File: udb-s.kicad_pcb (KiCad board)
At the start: 2 copper layers, 13 x 15.1 mm, 9 parts, among them J1 TYPE-C-31-M-12, J2 Conn_01x04, J3 Conn_01x04, U1 TPD4E05U06DQAR

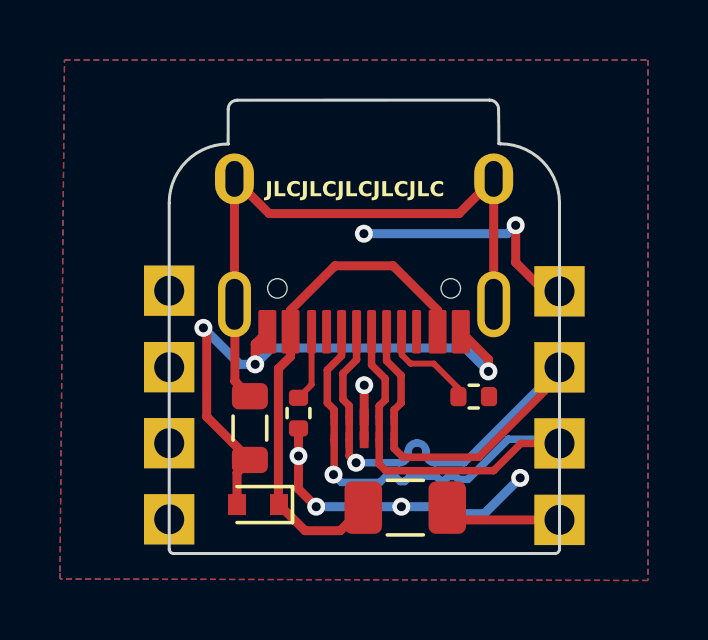
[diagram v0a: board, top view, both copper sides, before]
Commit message: Fuse Footprint update
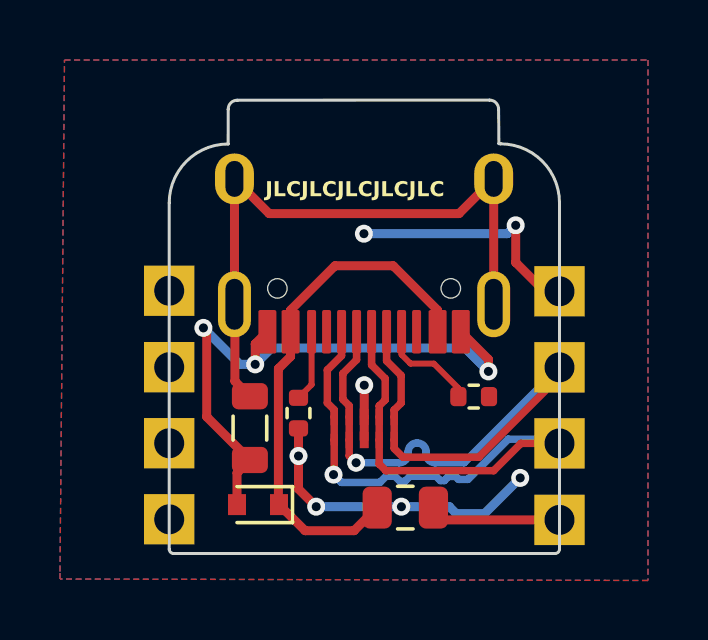
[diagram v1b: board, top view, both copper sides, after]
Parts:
- F1: footprint Fuse:Fuse_1206_3216Metric -> Fuse:Fuse_0805_2012Metric
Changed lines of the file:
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@@
 				(font
 					(size 1.27 1.27)
+					(thickness 0.15)
 				)
 			)
@@
 				(font
 					(size 1.27 1.27)
+					(thickness 0.15)
 				)
 			)
@@
 				(font
 					(size 1.27 1.27)
+					(thickness 0.15)
 				)
 			)
@@
 				(font
 					(size 1.27 1.27)
+					(thickness 0.15)
 				)
 			)
@@
 				(font
 					(size 1.27 1.27)
+					(thickness 0.15)
 				)
 			)
@@
 				(font
 					(size 1.27 1.27)
+					(thickness 0.15)
 				)
 			)
@@
 		)
 	)
-	(footprint "Fuse:Fuse_1206_3216Metric"
+	(footprint "Fuse:Fuse_0805_2012Metric"
 		(layer "F.Cu")
 		(at 130.66 90.42)
-		(descr "Fuse SMD 1206 (3216 Metric), square (rectangular) end terminal, IPC_7351 nominal, (Body size source: http://www.tortai-tech.com/upload/download/2011102023233369053.pdf), generated with kicad-footprint-generator")
+		(descr "Fuse SMD 0805 (2012 Metric), square (rectangular) end terminal, IPC_7351 nominal, (Body size source: https://docs.google.com/spreadsheets/d/1BsfQQcO9C6DZCsRaXUlFlo91Tg2WpOkGARC1WS5S8t0/edit?usp=sharing), generated with kicad-footprint-generator")
 		(tags "fuse")
 		(property "Reference" "F1"
-			(at 2.8 -1.1 0)
+			(at 0 -1.65 0)
 			(layer "F.SilkS")
 			(hide yes)
 			(effects
 				(font
-					(size 0.8 0.8)
+					(size 1 1)
 					(thickness 0.15)
 				)
@@
 		)
 		(property "Value" "SMD0805-050-16V"
-			(at 0 1.82 0)
+			(at 0 1.65 0)
 			(layer "F.Fab")
 			(effects
@@
 			)
 		)
-		(property "Footprint" "Fuse:Fuse_1206_3216Metric"
+		(property "Footprint" "Fuse:Fuse_0805_2012Metric"
 			(at 0 0 0)
 			(unlocked yes)
@@
 				(font
 					(size 1.27 1.27)
+					(thickness 0.15)
 				)
 			)
@@
 				(font
 					(size 1.27 1.27)
+					(thickness 0.15)
 				)
 			)
@@
 				(font
 					(size 1.27 1.27)
+					(thickness 0.15)
 				)
 			)
@@
 		(attr smd)
 		(fp_line
-			(start -0.602064 -0.91)
-			(end 0.602064 -0.91)
+			(start -0.258578 -0.71)
+			(end 0.258578 -0.71)
 			(stroke
 				(width 0.12)
@@
 		)
 		(fp_line
-			(start -0.602064 0.91)
-			(end 0.602064 0.91)
+			(start -0.258578 0.71)
+			(end 0.258578 0.71)
 			(stroke
 				(width 0.12)
@@
 		)
 		(fp_line
-			(start -2.28 -1.12)
-			(end 2.28 -1.12)
+			(start -1.68 -0.95)
+			(end 1.68 -0.95)
 			(stroke
 				(width 0.05)
@@
 		)
 		(fp_line
-			(start -2.28 1.12)
-			(end -2.28 -1.12)
+			(start -1.68 0.95)
+			(end -1.68 -0.95)
 			(stroke
 				(width 0.05)
@@
 		)
 		(fp_line
-			(start 2.28 -1.12)
-			(end 2.28 1.12)
+			(start 1.68 -0.95)
+			(end 1.68 0.95)
 			(stroke
 				(width 0.05)
@@
 		)
 		(fp_line
-			(start 2.28 1.12)
-			(end -2.28 1.12)
+			(start 1.68 0.95)
+			(end -1.68 0.95)
 			(stroke
 				(width 0.05)
@@
 		)
 		(fp_line
-			(start -1.6 -0.8)
-			(end 1.6 -0.8)
+			(start -1 -0.6)
+			(end 1 -0.6)
 			(stroke
 				(width 0.1)
@@
 		)
 		(fp_line
-			(start -1.6 0.8)
-			(end -1.6 -0.8)
+			(start -1 0.6)
+			(end -1 -0.6)
 			(stroke
 				(width 0.1)
@@
 		)
 		(fp_line
-			(start 1.6 -0.8)
-			(end 1.6 0.8)
+			(start 1 -0.6)
+			(end 1 0.6)
 			(stroke
 				(width 0.1)
@@
 		)
 		(fp_line
-			(start 1.6 0.8)
-			(end -1.6 0.8)
+			(start 1 0.6)
+			(end -1 0.6)
 			(stroke
 				(width 0.1)
@@
 		)
 		(fp_text user "${REFERENCE}"
-			(at -0.04 0.04 0)
+			(at 0 0 0)
 			(layer "F.Fab")
 			(effects
 				(font
-					(size 0.8 0.8)
-					(thickness 0.12)
+					(size 0.5 0.5)
+					(thickness 0.08)
 				)
 			)
 		)
 		(pad "1" smd roundrect
-			(at -1.4 0)
-			(size 1.25 1.75)
+			(at -0.9375 0)
+			(size 0.975 1.4)
 			(layers "F.Cu" "F.Paste" "F.Mask")
-			(roundrect_rratio 0.2)
+			(roundrect_rratio 0.25)
 			(net 2 "VBUS")
 			(pintype "passive")
 		)
 		(pad "2" smd roundrect
-			(at 1.4 0)
-			(size 1.25 1.75)
+			(at 0.9375 0)
+			(size 0.975 1.4)
 			(layers "F.Cu" "F.Paste" "F.Mask")
-			(roundrect_rratio 0.2)
+			(roundrect_rratio 0.25)
 			(net 9 "5V")
 			(pintype "passive")
 		)
-		(model "${KICAD6_3DMODEL_DIR}/Fuse.3dshapes/Fuse_1206_3216Metric.wrl"
+		(model "${KICAD8_3DMODEL_DIR}/Fuse.3dshapes/Fuse_0805_2012Metric.wrl"
 			(offset
 				(xyz 0 0 0)
@@
 				(font
 					(size 1.27 1.27)
+					(thickness 0.15)
 				)
 			)
@@
 				(font
 					(size 1.27 1.27)
+					(thickness 0.15)
 				)
 			)
@@
 				(font
 					(size 1.27 1.27)
+					(thickness 0.15)
 				)
 			)
@@
 				(font
 					(size 1.27 1.27)
+					(thickness 0.15)
 				)
 			)
@@
 				(font
 					(size 1.27 1.27)
+					(thickness 0.15)
 				)
 			)
@@
 				(font
 					(size 1.27 1.27)
+					(thickness 0.15)
 				)
 			)
@@
 				(font
 					(size 1.27 1.27)
+					(thickness 0.15)
 				)
 			)
@@
 				(font
 					(size 1.27 1.27)
+					(thickness 0.15)
 				)
 			)
@@
 				(font
 					(size 1.27 1.27)
+					(thickness 0.15)
 				)
 			)
@@
 				(font
 					(size 1.27 1.27)
+					(thickness 0.15)
 				)
 			)
@@
 				(font
 					(size 1.27 1.27)
+					(thickness 0.15)
 				)
 			)
@@
 				(font
 					(size 1.27 1.27)
+					(thickness 0.15)
 				)
 			)
@@
 				(font
 					(size 1.27 1.27)
+					(thickness 0.15)
 				)
 			)
@@
 				(font
 					(size 1.27 1.27)
+					(thickness 0.15)
 				)
 			)
@@
 				(font
 					(size 1.27 1.27)
+					(thickness 0.15)
 				)
 			)
@@
 				(font
 					(size 1.27 1.27)
+					(thickness 0.15)
 				)
 			)
@@
 				(font
 					(size 1.27 1.27)
+					(thickness 0.15)
 				)
 			)
@@
 				(font
 					(size 1.27 1.27)
+					(thickness 0.15)
 				)
 			)
@@
 	)
 	(segment
-		(start 128.49 91.19)
-		(end 129.26 90.42)
-		(width 0.3)
-		(layer "F.Cu")
-		(net 2)
-	)
-	(segment
 		(start 126.43 90.3)
 		(end 126.45 90.32)
@@
 	)
 	(segment
-		(start 126.836 84.5585)
-		(end 126.836 85.384)
+		(start 126.45 90.32)
+		(end 127.32 91.19)
 		(width 0.3)
 		(layer "F.Cu")
@@
 	)
 	(segment
-		(start 127.32 91.19)
-		(end 128.49 91.19)
+		(start 126.836 84.5585)
+		(end 126.836 85.384)
 		(width 0.3)
 		(layer "F.Cu")
@@
 	)
 	(segment
-		(start 126.45 90.32)
-		(end 127.32 91.19)
+		(start 126.43 85.79)
+		(end 126.43 90.3)
 		(width 0.3)
 		(layer "F.Cu")
@@
 	)
 	(segment
-		(start 126.43 85.79)
-		(end 126.43 90.3)
+		(start 128.9525 91.19)
+		(end 129.7225 90.42)
 		(width 0.3)
 		(layer "F.Cu")
@@
 	)
 	(segment
+		(start 127.32 91.19)
+		(end 128.9525 91.19)
+		(width 0.3)
+		(layer "F.Cu")
+		(net 2)
+	)
+	(segment
 		(start 128.31555 82.36)
 		(end 130.25645 82.36)
@@
 	)
 	(segment
-		(start 132.47 90.83)
-		(end 132.06 90.42)
+		(start 132.0075 90.83)
+		(end 131.5975 90.42)
 		(width 0.3)
 		(layer "F.Cu")
@@
 	(segment
 		(start 135.8 90.83)
-		(end 132.47 90.83)
+		(end 132.0075 90.83)
 		(width 0.3)
 		(layer "F.Cu")
